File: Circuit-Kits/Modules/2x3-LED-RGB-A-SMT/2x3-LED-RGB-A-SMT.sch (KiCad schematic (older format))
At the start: 1 part

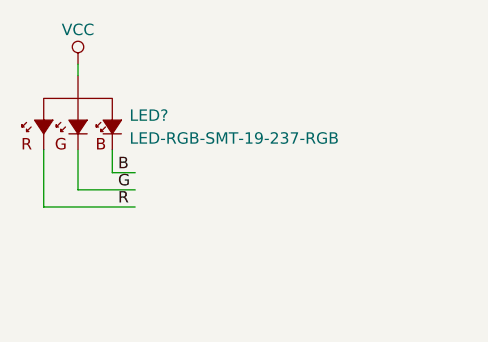
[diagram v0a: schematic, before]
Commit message: Add resistors to 2x3 LED RGB A 1.1
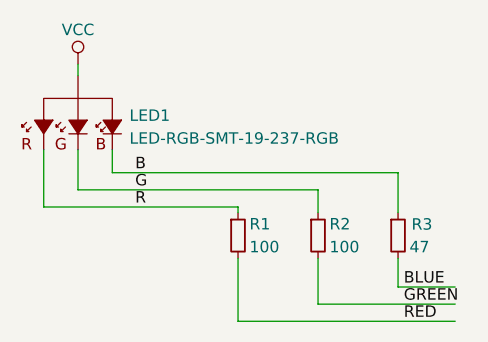
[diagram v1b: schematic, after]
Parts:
- added R1, R2: 100, Crazy_NonLego:RLC-0603-SMD, symbol RES-100-1%-1/10W-0603
- added R3: 47, Crazy_NonLego:RLC-0603-SMD, symbol RES-47-OHM-5%-1/10W-0603
- gave numbers to parts that had none: 1
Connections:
- net labels added: BLUE, GREEN, RED
- wire segments 7 -> 16
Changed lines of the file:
@@
 EESchema Schematic File Version 2
 LIBS:crazy_circuits
+LIBS:2x3-LED-RGB-A-SMT-cache
 EELAYER 25 0
 EELAYER END
@@
 $EndDescr
 $Comp
-L VCC #PWR?
+L VCC #PWR1
 U 1 1 5AE777B7
 P 4750 3450
-F 0 "#PWR?" H 4750 3300 50  0001 C CNN
+F 0 "#PWR1" H 4750 3300 50  0001 C CNN
 F 1 "VCC" H 4750 3600 50  0000 C CNN
 F 2 "" H 4750 3450 50  0000 C CNN
@@
 	4900 3825 4900 3925
 Wire Wire Line
-	4900 3925 5000 3925
+	4900 3925 6150 3925
 Wire Wire Line
 	4750 3825 4750 4000
 Wire Wire Line
-	4750 4000 5000 4000
+	4750 4000 5800 4000
 Wire Wire Line
 	4600 3825 4600 4075
 Wire Wire Line
-	4600 4075 5000 4075
-Text Label 4925 3925 0    50   ~ 0
-B
-Text Label 4925 4000 0    50   ~ 0
-G
-Text Label 4925 4075 0    50   ~ 0
-R
+	4600 4075 5450 4075
+Text Label 6175 4575 0    50   ~ 0
+RED
 $Comp
-L LED-RGB-SMT-19-237-RGB LED?
+L LED-RGB-SMT-19-237-RGB LED1
 U 1 1 5AE77B2A
 P 4900 3725
-F 0 "LED?" H 4975 3775 50  0000 L CNN
+F 0 "LED1" H 4975 3775 50  0000 L CNN
 F 1 "LED-RGB-SMT-19-237-RGB" H 4975 3675 50  0000 L CNN
 F 2 "Crazy_Circuits:LED-RGB-0606-19-237-2x3" H 4900 3375 50  0001 C CIN
@@
 	1    0    0    -1
 $EndComp
+$Comp
+L RES-100-1%-1/10W-0603 R1
+U 1 1 5AFB7418
+P 5450 4200
+F 0 "R1" H 5500 4250 50  0000 L CNN
+F 1 "100" H 5500 4150 50  0000 L CNN
+F 2 "Crazy_NonLego:RLC-0603-SMD" H 5450 3850 50  0001 C CIN
+F 3 "http://www.te.com/commerce/DocumentDelivery/DDEController?Action=srchrtrv&DocNm=1773204&DocType=DS&DocLang=English" H 5450 4200 5   0001 C CNN
+F 4 "RES SMD 100 OHM 1% 1/10W 0603" H 5450 3850 50  0001 C CIN "Description"
+F 5 "TE Conn" H 5450 3850 50  0001 C CIN "MF_Name"
+F 6 "CRG0603F100R" H 5450 3850 50  0001 C CIN "MF_PN"
+F 7 "Digikey" H 5450 3850 50  0001 C CIN "S1_Name"
+F 8 "A106047CT-ND" H 5450 3850 50  0001 C CIN "S1_PN"
+	1    5450 4200
+	1    0    0    -1
+$EndComp
+$Comp
+L RES-100-1%-1/10W-0603 R2
+U 1 1 5AFB7498
+P 5800 4200
+F 0 "R2" H 5850 4250 50  0000 L CNN
+F 1 "100" H 5850 4150 50  0000 L CNN
+F 2 "Crazy_NonLego:RLC-0603-SMD" H 5800 3850 50  0001 C CIN
+F 3 "http://www.te.com/commerce/DocumentDelivery/DDEController?Action=srchrtrv&DocNm=1773204&DocType=DS&DocLang=English" H 5800 4200 5   0001 C CNN
+F 4 "RES SMD 100 OHM 1% 1/10W 0603" H 5800 3850 50  0001 C CIN "Description"
+F 5 "TE Conn" H 5800 3850 50  0001 C CIN "MF_Name"
+F 6 "CRG0603F100R" H 5800 3850 50  0001 C CIN "MF_PN"
+F 7 "Digikey" H 5800 3850 50  0001 C CIN "S1_Name"
+F 8 "A106047CT-ND" H 5800 3850 50  0001 C CIN "S1_PN"
+	1    5800 4200
+	1    0    0    -1
+$EndComp
+$Comp
+L RES-47-OHM-5%-1/10W-0603 R3
+U 1 1 5AFB74D1
+P 6150 4200
+F 0 "R3" H 6209 4249 50  0000 L CNN
+F 1 "47" H 6200 4150 50  0000 L CNN
+F 2 "Crazy_NonLego:RLC-0603-SMD" H 6150 3850 50  0001 C CIN
+F 3 "http://www.yageo.com.tw/exep/pages/download/literatures/PYu-R_INT-thick_7.pdf" H 6150 4200 5   0001 C CNN
+F 4 "RES 47 OHM 5% 1/10W 0603" H 6150 3850 50  0001 C CIN "Description"
+F 5 "Yageo" H 6150 3850 50  0001 C CIN "MF_Name"
+F 6 "RC0603JR-0747RL" H 6150 3850 50  0001 C CIN "MF_PN"
+F 7 "Digikey" H 6150 3850 50  0001 C CIN "S1_Name"
+F 8 "311-47GRCT-ND" H 6150 3850 50  0001 C CIN "S1_PN"
+	1    6150 4200
+	1    0    0    -1
+$EndComp
+Wire Wire Line
+	6150 3925 6150 4100
+Wire Wire Line
+	5800 4000 5800 4100
+Wire Wire Line
+	5450 4075 5450 4100
+Wire Wire Line
+	5450 4300 5450 4575
+Wire Wire Line
+	6150 4300 6150 4425
+Wire Wire Line
+	5800 4300 5800 4500
+Wire Wire Line
+	5450 4575 6400 4575
+Wire Wire Line
+	5800 4500 6400 4500
+Wire Wire Line
+	6150 4425 6400 4425
+Text Label 6175 4500 0    50   ~ 0
+GREEN
+Text Label 6175 4425 0    50   ~ 0
+BLUE
+Text Label 5000 3925 0    50   ~ 0
+B
+Text Label 5000 4000 0    50   ~ 0
+G
+Text Label 5000 4075 0    50   ~ 0
+R
 $EndSCHEMATC

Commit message: Changed part number, no rev.
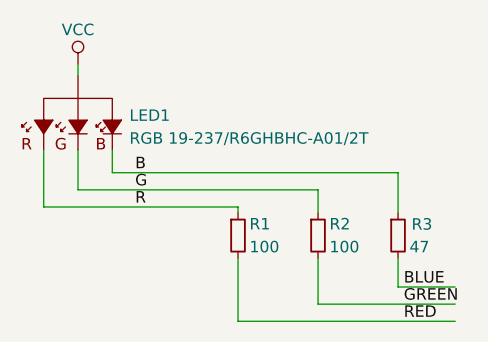
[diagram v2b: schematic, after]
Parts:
- LED1: value LED-RGB-SMT-19-237-RGB -> RGB 19-237/R6GHBHC-A01/2T; Description LED CHIP RGB 19-237 0606 SMD -> LED CHIP RGB 19-237 A01/2T SMD; MF_PN 19-237/R6GHBHC-A07/2T -> 19-237/R6GHBHC-A01/2T; S1_PN 1080-1590-1-ND -> 19-237/R6GHBHC-A01/2T-ND
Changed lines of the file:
@@
 RED
-$Comp
-L LED-RGB-SMT-19-237-RGB LED1
-U 1 1 5AE77B2A
-P 4900 3725
-F 0 "LED1" H 4975 3775 50  0000 L CNN
-F 1 "LED-RGB-SMT-19-237-RGB" H 4975 3675 50  0000 L CNN
-F 2 "Crazy_Circuits:LED-RGB-0606-19-237-2x3" H 4900 3375 50  0001 C CIN
-F 3 "http://erp.fastbom.com/uploads/p_dn/info/558513/19-237-R6GHBHC-A01-2T-139.pdf" H 4900 3725 5   0001 C CNN
-F 4 "LED CHIP RGB 19-237 0606 SMD " H 4900 3375 50  0001 C CIN "Description"
-F 5 "Digikey" H 4900 3375 50  0001 C CIN "MF_Name"
-F 6 "19-237/R6GHBHC-A07/2T" H 4900 3375 50  0001 C CIN "MF_PN"
-F 7 "Digikey" H 4900 3375 50  0001 C CIN "S1_Name"
-F 8 "1080-1590-1-ND" H 4900 3375 50  0001 C CIN "S1_PN"
-	1    4900 3725
-	1    0    0    -1
-$EndComp
 $Comp
 L RES-100-1%-1/10W-0603 R1
@@
 Text Label 5000 4075 0    50   ~ 0
 R
+$Comp
+L LED-RGB-SMT-19-237-RGB LED1
+U 1 1 5B0FF9DD
+P 4900 3725
+F 0 "LED1" H 4975 3775 50  0000 L CNN
+F 1 "RGB 19-237/R6GHBHC-A01/2T" H 4975 3675 50  0000 L CNN
+F 2 "Crazy_Circuits:LED-RGB-0606-19-237-2x3" H 4900 3375 50  0001 C CIN
+F 3 "http://erp.fastbom.com/uploads/p_dn/info/558513/19-237-R6GHBHC-A01-2T-139.pdf" H 4900 3725 5   0001 C CNN
+F 4 "LED CHIP RGB 19-237 A01/2T SMD " H 4900 3375 50  0001 C CIN "Description"
+F 5 "Digikey" H 4900 3375 50  0001 C CIN "MF_Name"
+F 6 "19-237/R6GHBHC-A01/2T" H 4900 3375 50  0001 C CIN "MF_PN"
+F 7 "Digikey" H 4900 3375 50  0001 C CIN "S1_Name"
+F 8 "19-237/R6GHBHC-A01/2T-ND" H 4900 3375 50  0001 C CIN "S1_PN"
+	1    4900 3725
+	1    0    0    -1
+$EndComp
 $EndSCHEMATC

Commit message: Port project to KiCad 5.0
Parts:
- LED1: symbol LED-RGB-SMT-19-237-RGB -> crazy_circuits:LED-RGB-SMT-19-237-RGB
- R1, R2: symbol RES-100-1%-1/10W-0603 -> crazy_circuits:RES-100-1%-1/10W-0603
- R3: symbol RES-47-OHM-5%-1/10W-0603 -> crazy_circuits:RES-47-OHM-5%-1/10W-0603
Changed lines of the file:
@@
-EESchema Schematic File Version 2
+EESchema Schematic File Version 4
 LIBS:crazy_circuits
-LIBS:2x3-LED-RGB-A-SMT-cache
-EELAYER 25 0
+EELAYER 26 0
 EELAYER END
 $Descr USLetter 11000 8500
@@
 $EndDescr
 $Comp
-L VCC #PWR1
+L crazy_circuits:VCC #PWR1
 U 1 1 5AE777B7
 P 4750 3450
@@
 RED
 $Comp
-L RES-100-1%-1/10W-0603 R1
+L crazy_circuits:RES-100-1%-1/10W-0603 R1
 U 1 1 5AFB7418
 P 5450 4200
@@
 $EndComp
 $Comp
-L RES-100-1%-1/10W-0603 R2
+L crazy_circuits:RES-100-1%-1/10W-0603 R2
 U 1 1 5AFB7498
 P 5800 4200
@@
 $EndComp
 $Comp
-L RES-47-OHM-5%-1/10W-0603 R3
+L crazy_circuits:RES-47-OHM-5%-1/10W-0603 R3
 U 1 1 5AFB74D1
 P 6150 4200
@@
 R
 $Comp
-L LED-RGB-SMT-19-237-RGB LED1
+L crazy_circuits:LED-RGB-SMT-19-237-RGB LED1
 U 1 1 5B0FF9DD
 P 4900 3725
